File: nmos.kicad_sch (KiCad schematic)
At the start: 0 parts

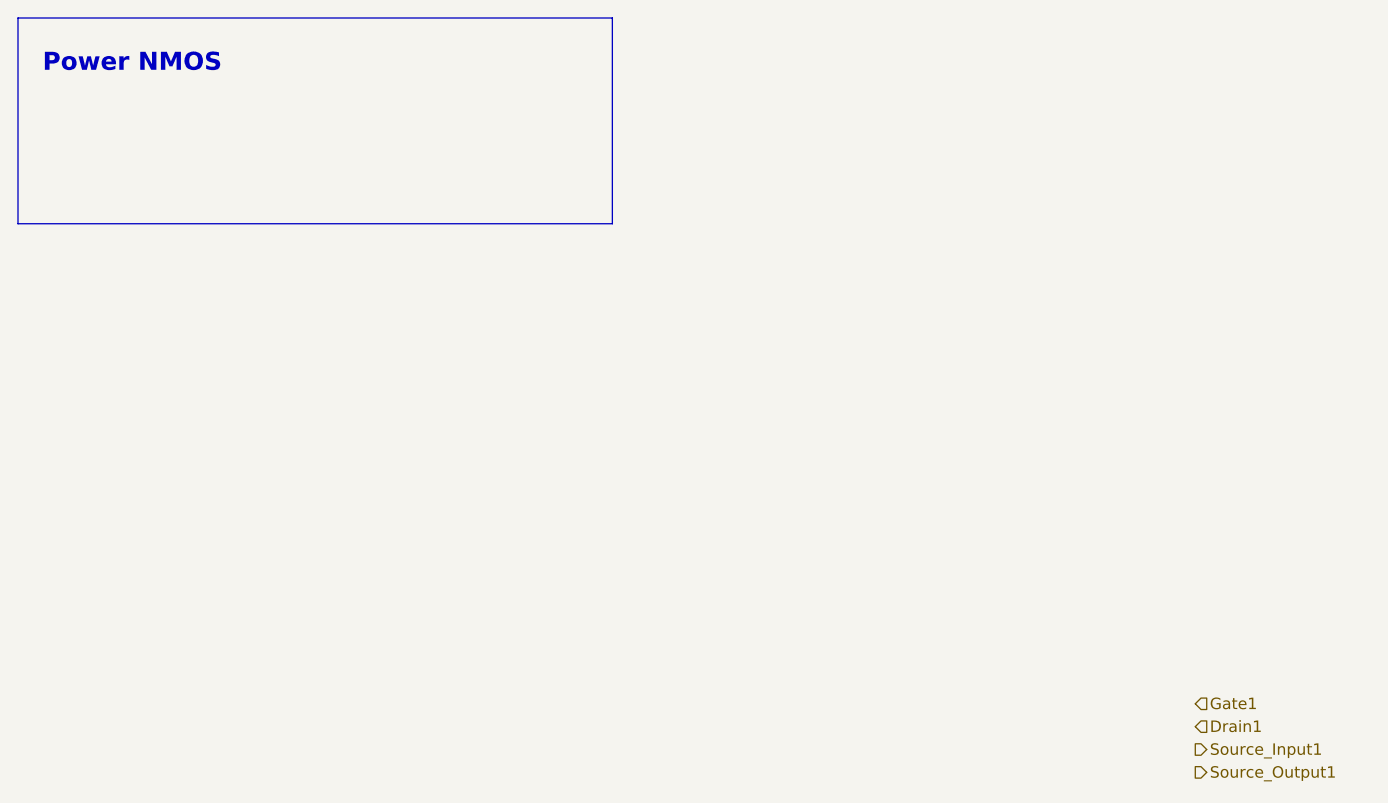
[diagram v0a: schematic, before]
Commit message: added circuitry for sch
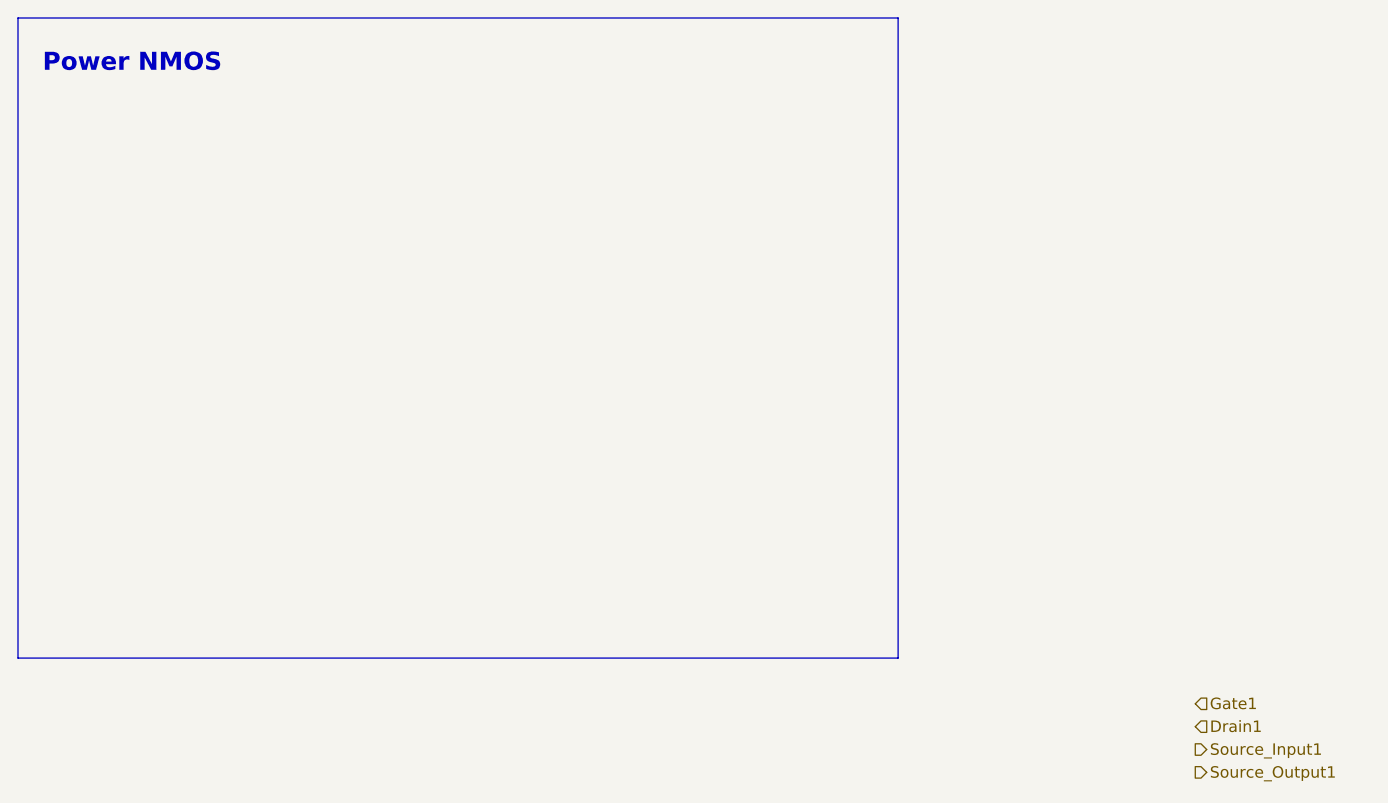
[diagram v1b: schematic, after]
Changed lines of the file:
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@@
 	(rectangle
 		(start 12.7 12.7)
-		(end 78.74 35.56)
+		(end 110.49 83.82)
 		(stroke
 			(width 0)
